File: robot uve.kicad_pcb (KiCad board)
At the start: 2 copper layers, 100 x 100 mm, 60 parts, among them J1 pulsador1, J10 HC-SR04, J11 HC-SR04, J12 HC-SR04, J13 TB_1X3, J14 I2C_B, J15 I2C_C, J16 NeoPixel, J17 neopixel, J18 +5V IN, J19 GND, J2 I2C_A, J20 pulsador2, J21 IR, J3 TB_1X3, J4 comunicacion a rpi, J5 12V IN, J6 GND, J7 HC-SR04, J8 HC-SR04, J9 HC-SR04, K1 RELAY_C, K3 RELAY_C, P1 Digital, P10 CONN_01X01, P11 CONN_01X01, P12 CONN_01X01, P13 CONN_01X01, P14 motor3, P15 motor2, P16 Sensores de Linea, P17 motor1, P18 motor4, P2 Power, P3 Analog, P4 Analog, P5 PWM, P6 PWM, P7 Communication, P8 CONN_01X01, P9 CONN_01X01, Q1 2N7002, Q3 2N7002, Q4 2N7002

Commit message: se modifico archicos de fabricacion
se modifico archivos de fabricaciony se mejoro el pcb
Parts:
- moved Q3 6.60 mm to (164.6, 73.4), turned to 180 degrees
- moved G*** 1.80 mm to (149.4, 95.4)
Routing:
- net +5V: track 426.2 -> 404.4 mm, vias 0 -> 2
- net GND: track 65.4 -> 57.2 mm
- net /49: track 6.83 -> 8.37 mm
- net /12V: track 118.6 -> 119.3 mm
- net Net-(D4-Pad1): track 9.23 -> 9.77 mm
- net /A10: track 14.1 -> 14.6 mm

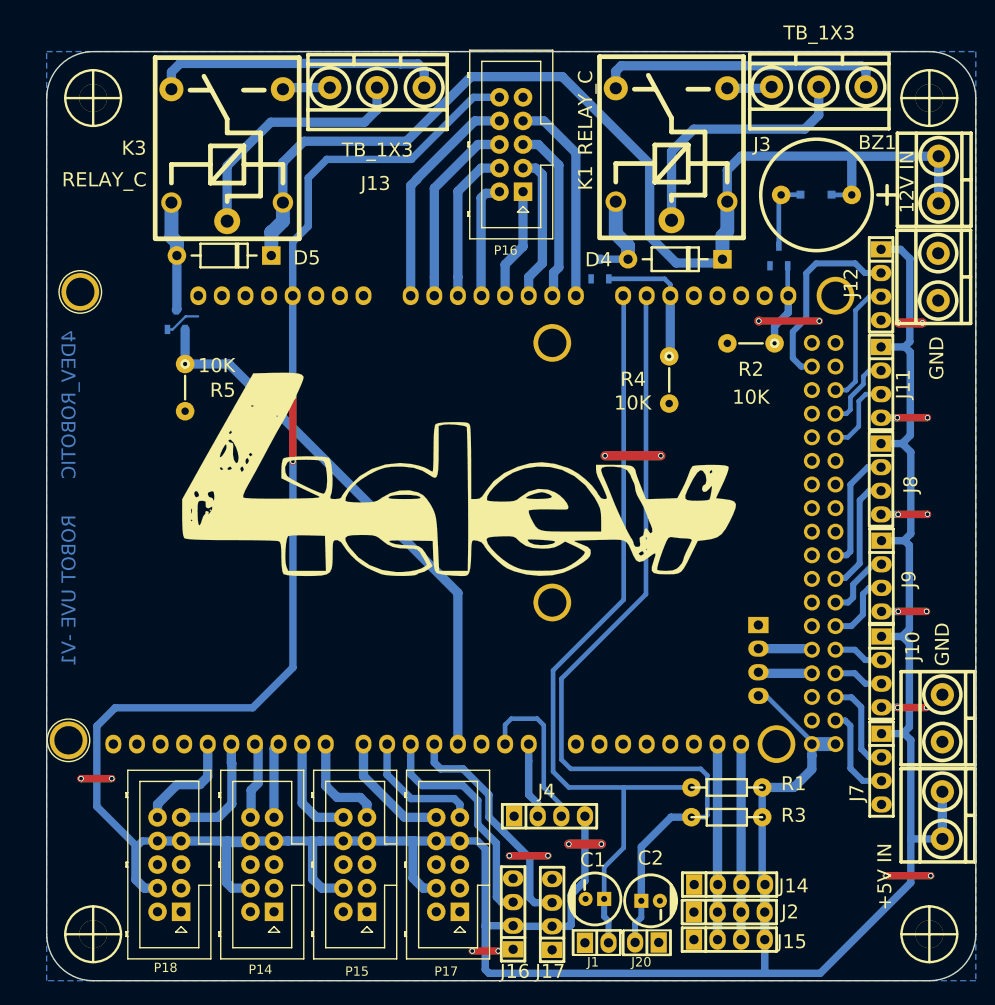
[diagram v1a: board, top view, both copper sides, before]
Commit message: modificacion en el pcb
se modifico el pcb
se agrego boton reset
se modifico seregrafia
se modifico vias
y se agrego archicos BOM
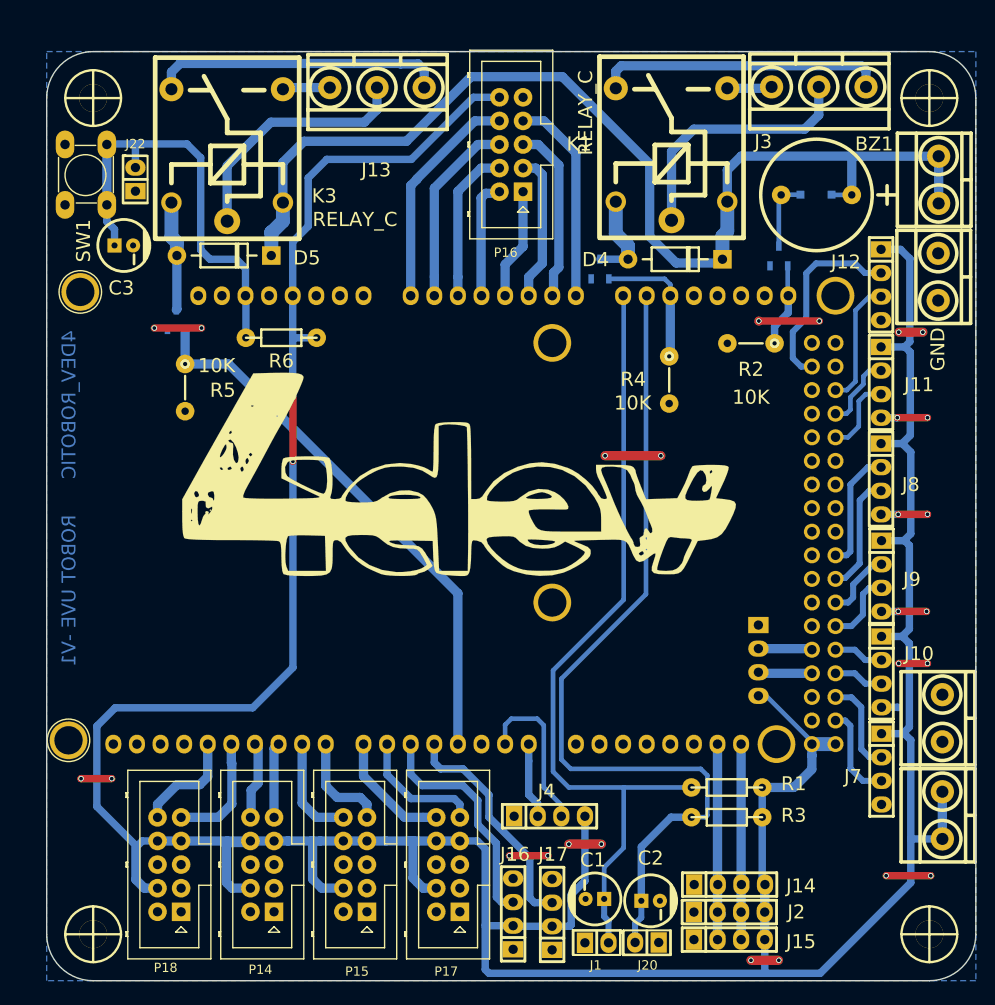
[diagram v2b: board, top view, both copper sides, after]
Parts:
- added C3: 10uf, EESTN5:CAP_ELEC_5x11mm, F.Cu at (113.3, 70.9)
- added G***: LOGO, EESTN5:LOGO_4DEV1, B.Cu at (145.3, 95.0)
- added J22: pulsador2, EESTN5:Pin_Header_2, F.Cu at (114.2, 63.8)
- added R6: 10k, EESTN5:RES0.3, F.Cu at (130.2, 80.8)
- added SW1: RESET, EESTN5:Pulsador_TH_4, F.Cu at (109.2, 63.2)
- J13, J3: value TB_1X3 -> NC - C - NA
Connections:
- P1 pad 11: (no net) -> /44
- P1 pad 12: (no net) -> /45
- P1 pad 13: (no net) -> /42
- P1 pad 14: (no net) -> /43
- P1 pad 15: (no net) -> /40
- P1 pad 16: (no net) -> /41
- P1 pad 17: (no net) -> /38
- P1 pad 18: (no net) -> /39
- P1 pad 19: (no net) -> /36
- P1 pad 21: (no net) -> /34
- P1 pad 23: (no net) -> /32
- P1 pad 25: (no net) -> /30
- P1 pad 31: (no net) -> /24
- P1 pad 33: (no net) -> /22
- P1 pad 4: (no net) -> /53(SS)
- P1 pad 5: (no net) -> /50(MISO)
- P1 pad 7: (no net) -> /48
- P1 pad 9: (no net) -> /46
- P10 pad 1: (no net) -> Net-(P10-Pad1)
- P11 pad 1: (no net) -> Net-(P11-Pad1)
- P12 pad 1: (no net) -> Net-(P12-Pad1)
- P13 pad 1: (no net) -> Net-(P13-Pad1)
- P14 pad 1: (no net) -> Net-(P14-Pad1)
- P14 pad 2: (no net) -> Net-(P14-Pad2)
- P14 pad 5: (no net) -> Net-(P14-Pad5)
- P14 pad 6: (no net) -> Net-(P14-Pad6)
- P15 pad 1: (no net) -> Net-(P15-Pad1)
- P15 pad 2: (no net) -> Net-(P15-Pad2)
- P15 pad 5: (no net) -> Net-(P15-Pad5)
- P15 pad 6: (no net) -> Net-(P15-Pad6)
- P17 pad 1: (no net) -> Net-(P17-Pad1)
- P17 pad 2: (no net) -> Net-(P17-Pad2)
- P17 pad 5: (no net) -> Net-(P17-Pad5)
- P17 pad 6: (no net) -> Net-(P17-Pad6)
- P18 pad 1: (no net) -> Net-(P18-Pad1)
- P18 pad 2: (no net) -> Net-(P18-Pad2)
- P18 pad 5: (no net) -> Net-(P18-Pad5)
- P18 pad 6: (no net) -> Net-(P18-Pad6)
- P2 pad 1: (no net) -> Net-(P2-Pad1)
- P2 pad 2: (no net) -> /IOREF
- P2 pad 3: (no net) -> /Reset
- P2 pad 4: (no net) -> +3V3
- P2 pad 8: (no net) -> /Vin
- P4 pad 4: (no net) -> /A11
- P4 pad 5: (no net) -> /A12
- P4 pad 6: (no net) -> /A13
- P4 pad 7: (no net) -> /A14
- P5 pad 1: (no net) -> /SCL
- P5 pad 2: (no net) -> /SDA
- P5 pad 3: (no net) -> /AREF
- P6 pad 6: (no net) -> /2(**)
- P7 pad 1: (no net) -> /14(Tx3)
- P7 pad 2: (no net) -> /15(Rx3)
- P7 pad 3: (no net) -> /16(Tx2)
- P7 pad 4: (no net) -> /17(Rx2)
- P7 pad 5: (no net) -> /18(Tx1)
- P7 pad 6: (no net) -> /19(Rx1)
- P8 pad 1: (no net) -> Net-(P8-Pad1)
- P9 pad 1: (no net) -> Net-(P9-Pad1)
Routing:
- net /Reset: track 0.00 -> 48.4 mm
- net +5V: track 404.4 -> 407.0 mm
- net GND: track 57.2 -> 58.8 mm, vias 24 -> 26
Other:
- board text added: "5V+"
- board text added: "GND"

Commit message: Varios
Pase a SMD (1206) las resistencias.
Modifique una conexión a 5V para evitar un jumper.
Acomode un poco más la serigrafia (todavía falta).
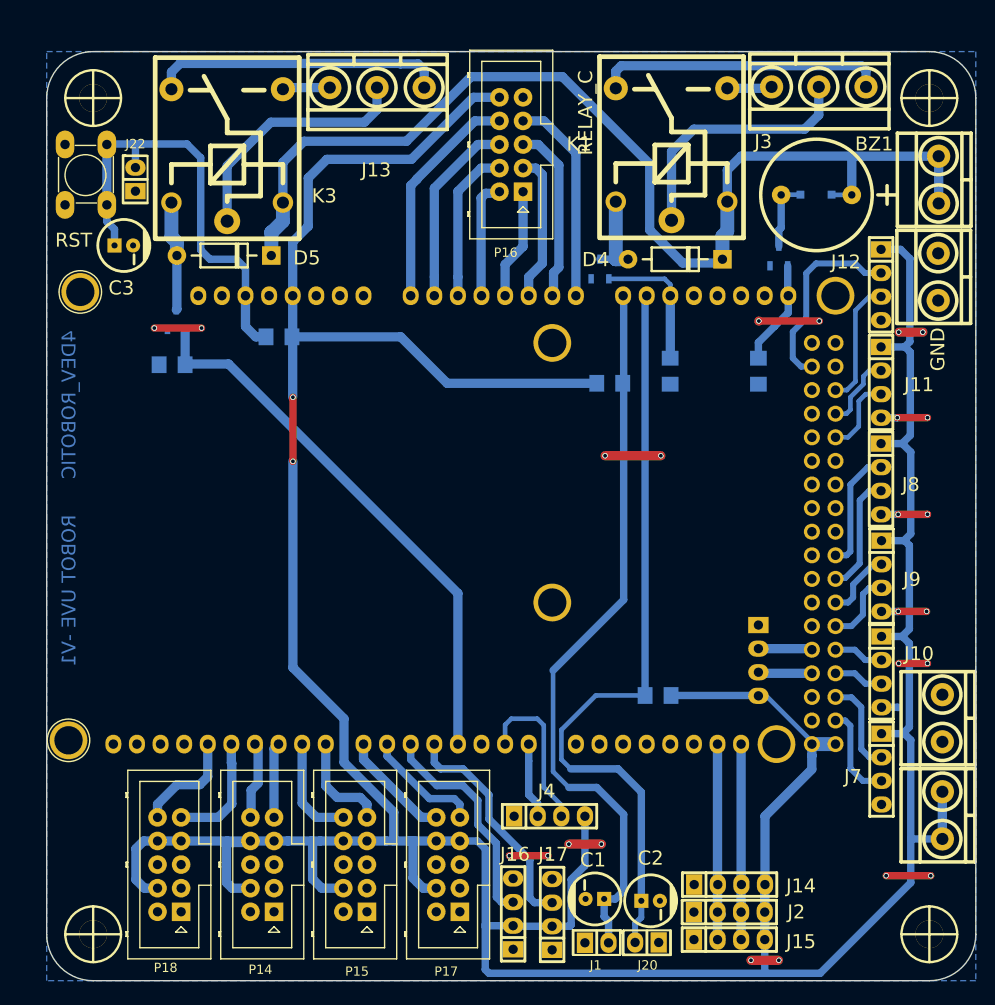
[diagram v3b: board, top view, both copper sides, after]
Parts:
- removed G*** (x2): LOGO, EESTN5:LOGO_4DEV1
- R1, R3, R6: footprint EESTN5:RES0.3 -> EESTN5:R_1206; moved to B.Cu
- R2, R4, R5: footprint EESTN5:RES0.2 -> EESTN5:R_1206; moved to B.Cu
- SW1: value RESET -> RST
- moved R1 45.3 mm to (165.6, 85.7)
- moved R3 15.0 mm to (170.8, 119.3), turned to 0 degrees
- moved R2 3.10 mm to (181.6, 84.4), turned to 90 degrees
- moved R5 2.83 mm to (118.5, 83.7), turned to 0 degrees
- moved R4 0.95 mm to (172.1, 84.4), turned to 90 degrees
- moved R6 0.27 mm to (130.0, 80.7), turned to 0 degrees
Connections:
- P1 pad 11: /44 -> (no net)
- P1 pad 12: /45 -> (no net)
- P1 pad 13: /42 -> (no net)
- P1 pad 14: /43 -> (no net)
- P1 pad 15: /40 -> (no net)
- P1 pad 16: /41 -> (no net)
- P1 pad 17: /38 -> (no net)
- P1 pad 18: /39 -> (no net)
- P1 pad 19: /36 -> (no net)
- P1 pad 21: /34 -> (no net)
- P1 pad 23: /32 -> (no net)
- P1 pad 25: /30 -> (no net)
- P1 pad 31: /24 -> (no net)
- P1 pad 33: /22 -> (no net)
- P1 pad 4: /53(SS) -> (no net)
- P1 pad 5: /50(MISO) -> (no net)
- P1 pad 7: /48 -> (no net)
- P1 pad 9: /46 -> (no net)
- P10 pad 1: Net-(P10-Pad1) -> (no net)
- P11 pad 1: Net-(P11-Pad1) -> (no net)
- P12 pad 1: Net-(P12-Pad1) -> (no net)
- P13 pad 1: Net-(P13-Pad1) -> (no net)
- P14 pad 1: Net-(P14-Pad1) -> (no net)
- P14 pad 2: Net-(P14-Pad2) -> (no net)
- P14 pad 5: Net-(P14-Pad5) -> (no net)
- P14 pad 6: Net-(P14-Pad6) -> (no net)
- P15 pad 1: Net-(P15-Pad1) -> (no net)
- P15 pad 2: Net-(P15-Pad2) -> (no net)
- P15 pad 5: Net-(P15-Pad5) -> (no net)
- P15 pad 6: Net-(P15-Pad6) -> (no net)
- P17 pad 1: Net-(P17-Pad1) -> (no net)
- P17 pad 2: Net-(P17-Pad2) -> (no net)
- P17 pad 5: Net-(P17-Pad5) -> (no net)
- P17 pad 6: Net-(P17-Pad6) -> (no net)
- P18 pad 1: Net-(P18-Pad1) -> (no net)
- P18 pad 2: Net-(P18-Pad2) -> (no net)
- P18 pad 5: Net-(P18-Pad5) -> (no net)
- P18 pad 6: Net-(P18-Pad6) -> (no net)
- P2 pad 1: Net-(P2-Pad1) -> (no net)
- P2 pad 2: /IOREF -> (no net)
- P2 pad 4: +3V3 -> (no net)
- P2 pad 8: /Vin -> (no net)
- P4 pad 4: /A11 -> (no net)
- P4 pad 5: /A12 -> (no net)
- P4 pad 6: /A13 -> (no net)
- P4 pad 7: /A14 -> (no net)
- P5 pad 1: /SCL -> (no net)
- P5 pad 2: /SDA -> (no net)
- P5 pad 3: /AREF -> (no net)
- P6 pad 6: /2(**) -> (no net)
- P7 pad 1: /14(Tx3) -> (no net)
- P7 pad 2: /15(Rx3) -> (no net)
- P7 pad 3: /16(Tx2) -> (no net)
- P7 pad 4: /17(Rx2) -> (no net)
- P7 pad 5: /18(Tx1) -> (no net)
- P7 pad 6: /19(Rx1) -> (no net)
- P8 pad 1: Net-(P8-Pad1) -> (no net)
- P9 pad 1: Net-(P9-Pad1) -> (no net)
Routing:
- net +5V: track 407.0 -> 431.0 mm
- net /A9: track 93.5 -> 84.0 mm
- net /A8: track 87.8 -> 79.5 mm
- net GND: track 58.8 -> 55.3 mm, vias 26 -> 24
- net /A15: track 8.98 -> 11.3 mm
- net /Reset: track 48.4 -> 49.9 mm
- net /6(**): track 13.9 -> 12.7 mm
- net /7(**): track 13.1 -> 12.1 mm
- net /5(**): track 24.9 -> 23.9 mm
- net Net-(D4-Pad1): track 9.77 -> 9.22 mm
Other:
- net class Default: trace_width 0.25 -> 0.5
- rule trace_min: 0.2 -> 0.5

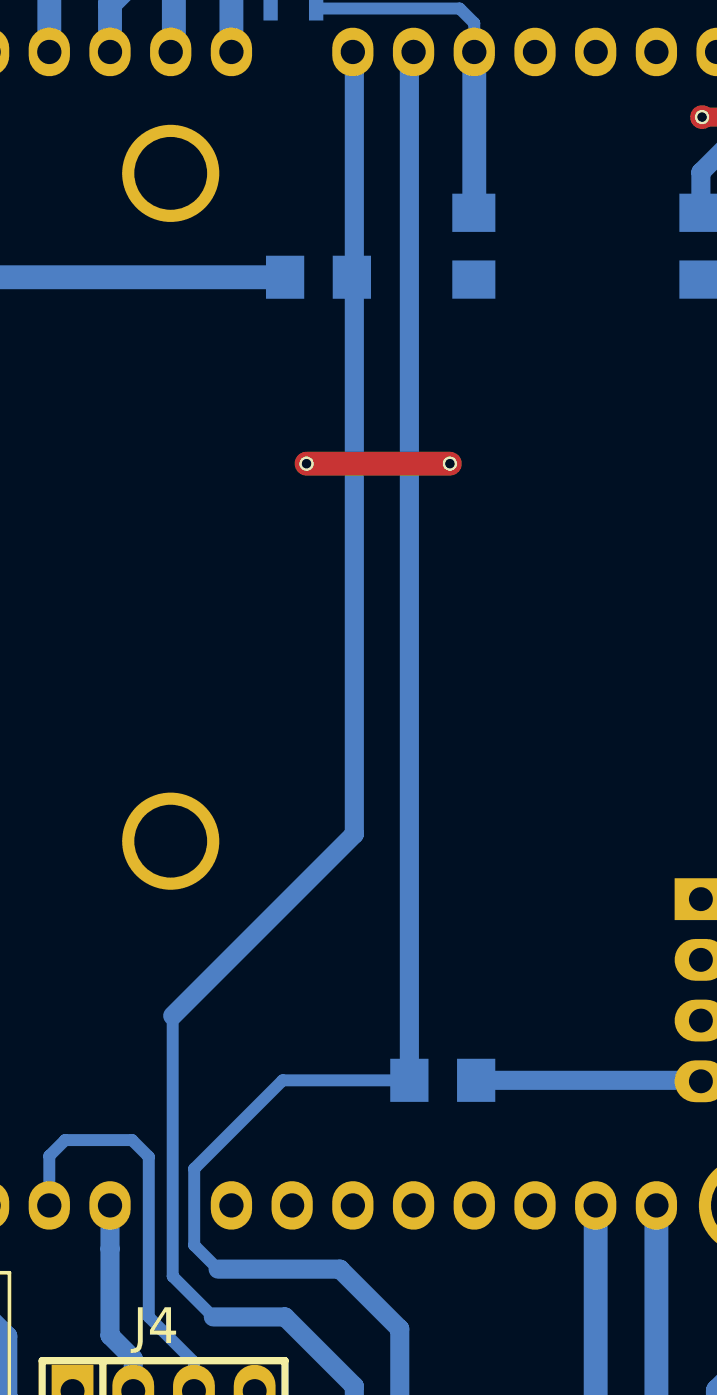
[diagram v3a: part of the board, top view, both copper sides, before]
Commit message: varios cambios
se agrega lista de componentes
se modifica el pcb
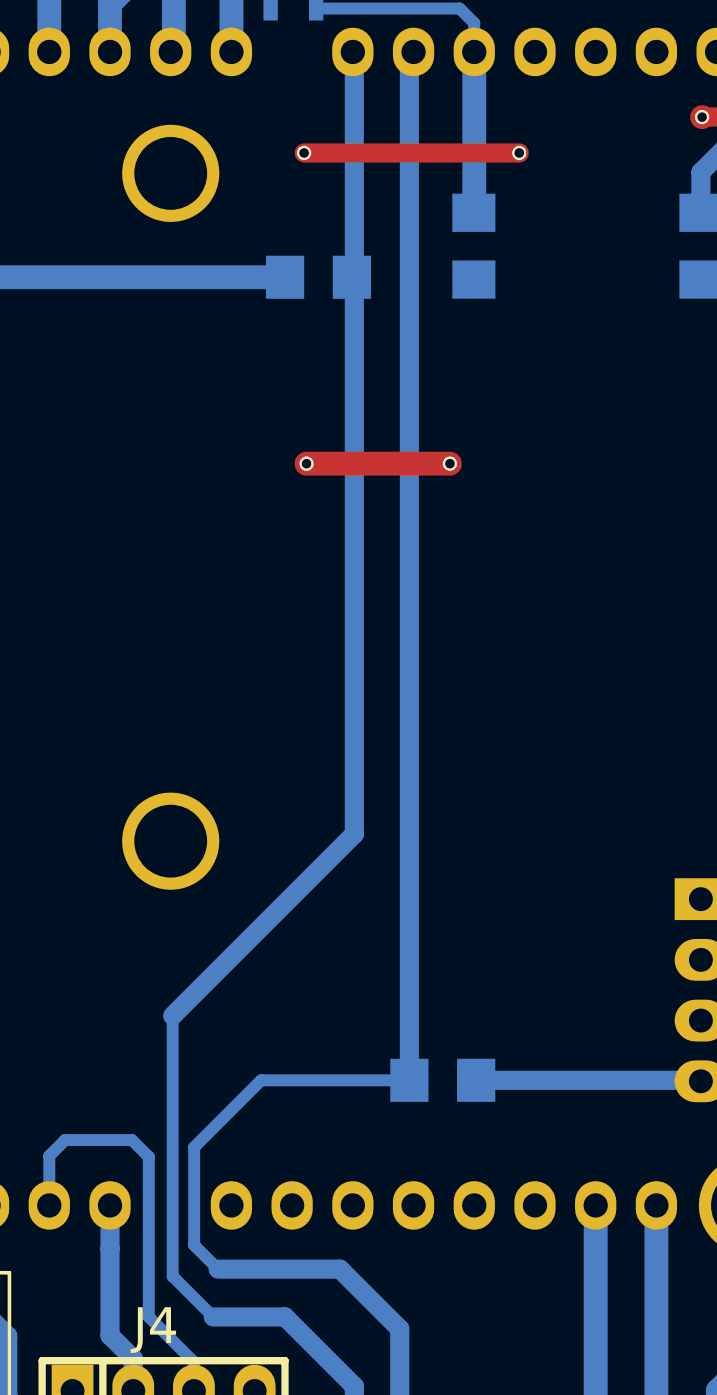
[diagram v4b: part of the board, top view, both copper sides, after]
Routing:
- net GND: track 55.3 -> 64.3 mm, vias 24 -> 26
- net /A9: track 84.0 -> 84.5 mm
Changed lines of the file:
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@@
-(kicad_pcb (version 20171130) (host pcbnew "(5.1.8)-1")
+(kicad_pcb (version 20171130) (host pcbnew 5.1.7-a382d34a8~87~ubuntu20.04.1)
   (general
     (thickness 1.6)
     (drawings 20)
-    (tracks 476)
+    (tracks 479)
     (zones 0)
     (modules 63)
@@
   )
   (setup
-    (last_trace_width 1)
+    (last_trace_width 0.8)
     (user_trace_width 0.5)
     (user_trace_width 0.65)
@@
   (via (at 199.8 89.4) (size 0.6) (drill 0.4) (layers F.Cu B.Cu) (net 1))
   (via (at 154.8 136.55) (size 0.6) (drill 0.4) (layers F.Cu B.Cu) (net 1))
-  (via (at 165.1 93.5) (size 0.6) (drill 0.4) (layers F.Cu B.Cu) (net 1))
-  (via (at 171.1 93.5) (size 0.6) (drill 0.4) (layers F.Cu B.Cu) (net 1))
   (via (at 188.15 79) (size 0.6) (drill 0.4) (layers F.Cu B.Cu) (net 1))
   (via (at 164.7 135.3) (size 0.6) (drill 0.4) (layers F.Cu B.Cu) (net 1))
@@
   (via (at 199.3 80.2) (size 0.6) (drill 0.4) (layers F.Cu B.Cu) (net 1))
   (segment (start 196.75 80.2) (end 199.3 80.2) (width 1) (layer F.Cu) (net 1))
-  (segment (start 171.1 93.5) (end 165.1 93.5) (width 1) (layer F.Cu) (net 1))
   (via (at 158.95 136.55) (size 0.6) (drill 0.4) (layers F.Cu B.Cu) (net 1))
   (segment (start 154.8 136.55) (end 158.95 136.55) (width 0.8) (layer F.Cu) (net 1))
@@
   (via (at 121.666 79.756) (size 0.6) (drill 0.4) (layers F.Cu B.Cu) (net 1))
   (segment (start 116.586 79.756) (end 121.666 79.756) (width 0.8) (layer F.Cu) (net 1))
+  (via (at 165 80.5) (size 0.6) (drill 0.4) (layers F.Cu B.Cu) (net 1))
+  (via (at 174 80.5) (size 0.6) (drill 0.4) (layers F.Cu B.Cu) (net 1))
+  (segment (start 171.1 93.5) (end 165.1 93.5) (width 1) (layer F.Cu) (net 1) (status 1000000))
+  (via (at 171.1 93.5) (size 0.6) (drill 0.4) (layers F.Cu B.Cu) (net 1) (status 1000000))
+  (via (at 165.1 93.5) (size 0.6) (drill 0.4) (layers F.Cu B.Cu) (net 1) (status 1000000))
+  (segment (start 165 80.5) (end 174 80.5) (width 0.8) (layer F.Cu) (net 1))
   (segment (start 193.05 73.83) (end 194.8 73.83) (width 0.65) (layer B.Cu) (net 2) (status 20))
   (segment (start 192.02 72.8) (end 193.05 73.83) (width 0.65) (layer B.Cu) (net 2))
@@
   (segment (start 169 141.4) (end 169 129.7) (width 0.8) (layer B.Cu) (net 51))
   (segment (start 169.5 76.352) (end 169.578 76.274) (width 0.5) (layer B.Cu) (net 51))
-  (segment (start 160.4 126.2) (end 160.4 123) (width 0.5) (layer B.Cu) (net 51))
-  (segment (start 161.4 127.2) (end 160.4 126.2) (width 0.5) (layer B.Cu) (net 51))
-  (segment (start 164.1 119.3) (end 169.903 119.3) (width 0.5) (layer B.Cu) (net 51))
-  (segment (start 160.4 123) (end 164.1 119.3) (width 0.5) (layer B.Cu) (net 51))
   (segment (start 169.403 76.449) (end 169.578 76.274) (width 0.5) (layer B.Cu) (net 51))
   (segment (start 169.403 119.3) (end 169.403 76.449) (width 0.8) (layer B.Cu) (net 51))
+  (segment (start 163.2 119.3) (end 169.903 119.3) (width 0.5) (layer B.Cu) (net 51))
+  (segment (start 160.4 122.1) (end 163.2 119.3) (width 0.5) (layer B.Cu) (net 51))
+  (segment (start 160.4 126.2) (end 160.4 122.1) (width 0.5) (layer B.Cu) (net 51))
+  (segment (start 161.4 127.2) (end 160.4 126.2) (width 0.5) (layer B.Cu) (net 51))
   (segment (start 187.244 114.26) (end 187.358 114.374) (width 1) (layer B.Cu) (net 52) (status 30))
   (segment (start 181.6 114.26) (end 187.244 114.26) (width 1) (layer B.Cu) (net 52) (status 30))
